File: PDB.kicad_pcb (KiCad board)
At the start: 2 copper layers, 50 x 80 mm, 98 parts, among them J1 Conn_01x02, J10 Conn_01x02_MountingPin, J11 USB_C_Receptacle_USB2.0, J2 Conn_01x02, J3 Conn_01x02, J4 Conn_01x02, J5 Conn_01x02, J6 Conn_01x02, J7 Conn_01x02, J8 Conn_01x02, J9 Conn_02x03_Odd_Even, SW1 SW_Push, U1 ATmega2560-16AU, U2 LMZM23600, U3 LTC2946, U4 FT230XQ, U5 LMZ13608, U6 LTC2946, Y1 16MHz

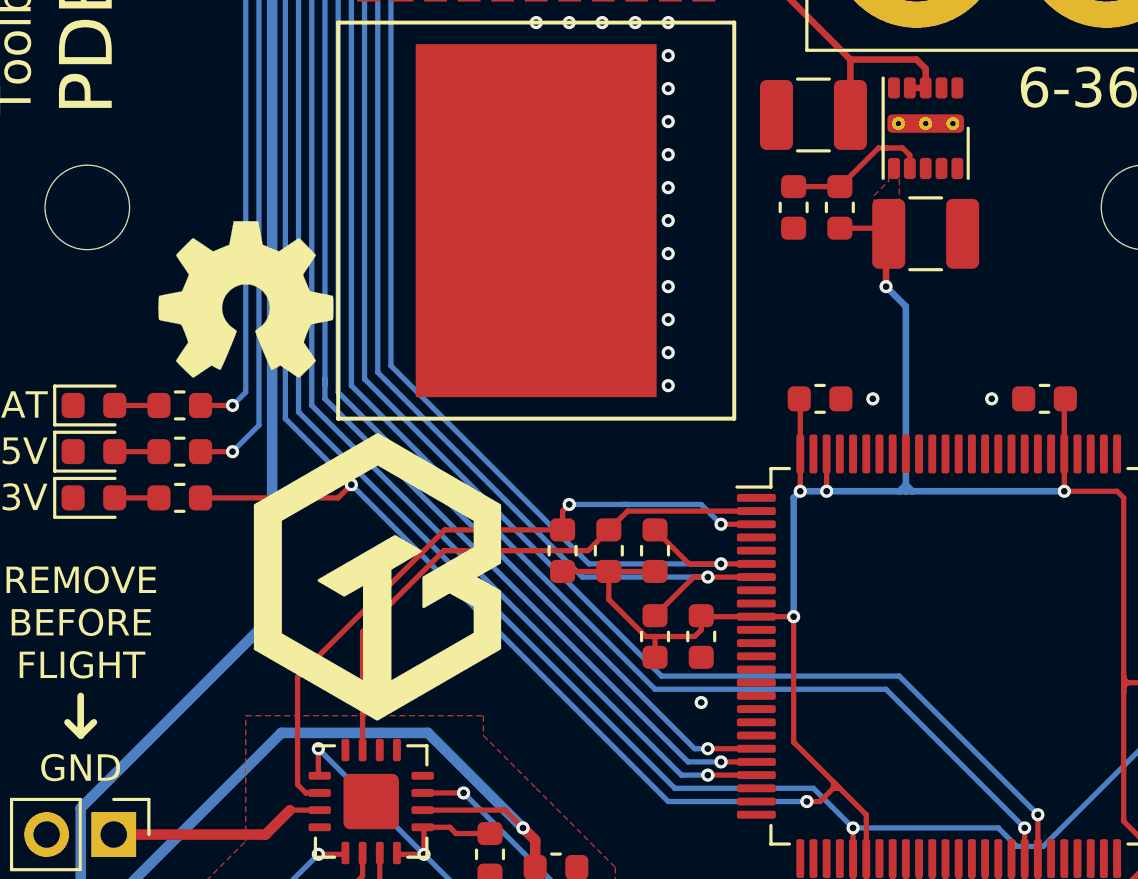
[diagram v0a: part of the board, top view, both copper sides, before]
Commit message: fix 3.3v regulator output cap
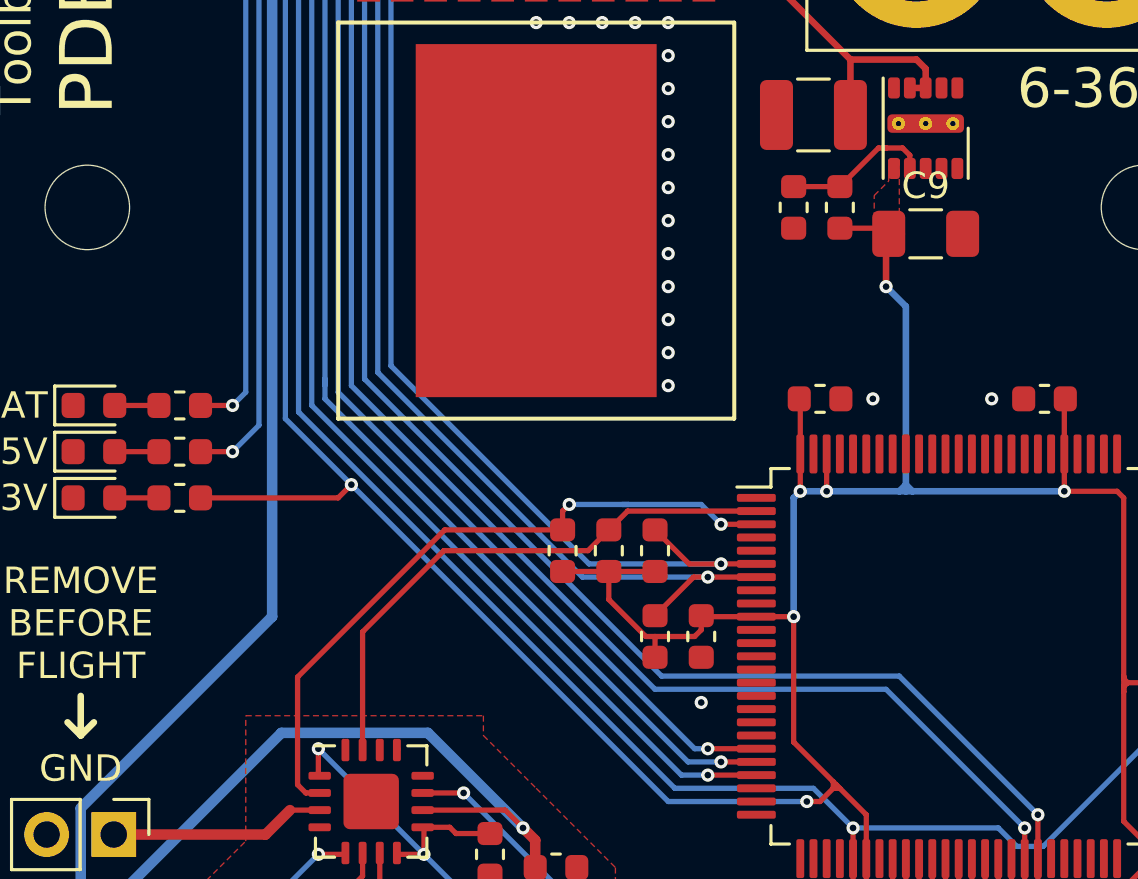
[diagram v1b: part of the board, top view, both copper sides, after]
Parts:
- removed REF**: OSHW-Symbol_6.7x6mm_SilkScreen, Symbol:OSHW-Symbol_6.7x6mm_SilkScreen
- removed REF**: ToolboxLogo_Large, Toolbox:ToolboxLogo_Large
- removed REF**: ToolboxLogo, Toolbox:ToolboxLogo
- C9: value 33µF -> 22µF; footprint Capacitor_SMD:C_1210_3225Metric -> Capacitor_SMD:C_1206_3216Metric

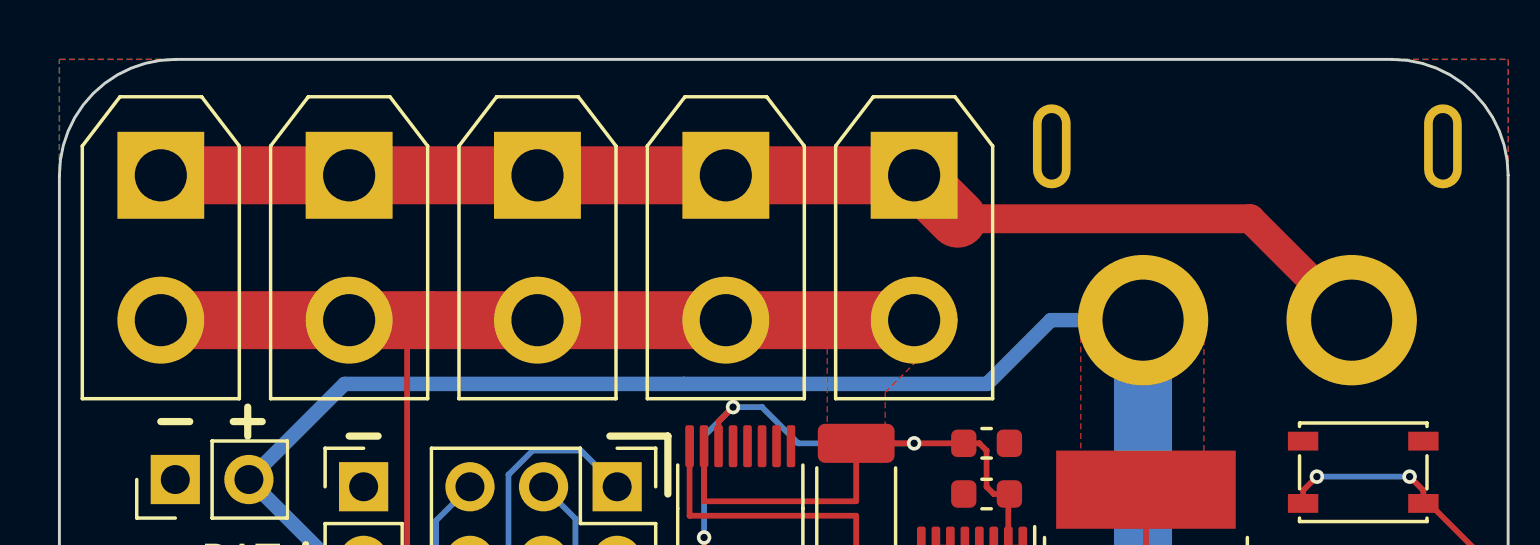
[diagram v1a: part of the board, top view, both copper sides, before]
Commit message: fix thermals for 5V out
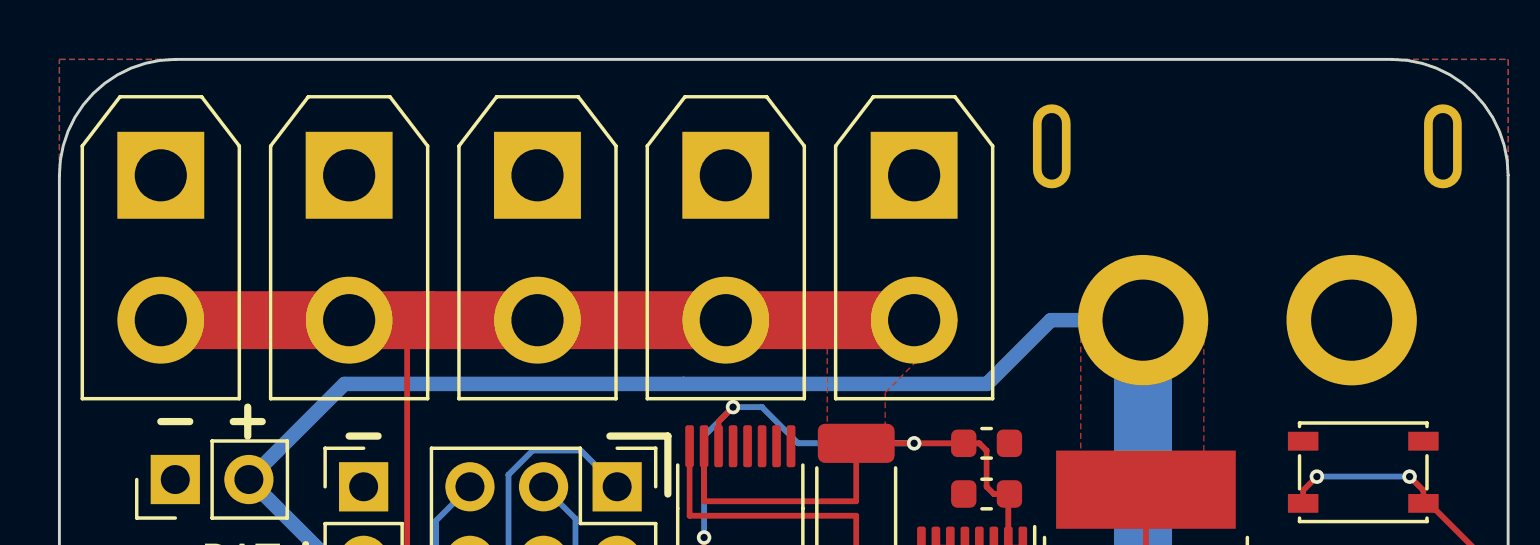
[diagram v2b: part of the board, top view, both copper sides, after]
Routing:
- net GND: track 43.2 -> 0.00 mm
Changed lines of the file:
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@@
     (thickness 1.6)
     (drawings 40)
-    (tracks 546)
+    (tracks 539)
     (zones 0)
     (modules 95)
@@
     (mod_text_size 1 1)
     (mod_text_width 0.25)
-    (pad_size 1.25 1.75)
-    (pad_drill 0)
+    (pad_size 3 3)
+    (pad_drill 1.8)
     (pad_to_mask_clearance 0)
     (solder_mask_min_width 0.25)
@@
       (net 21 +5V))
     (pad 1 thru_hole rect (at 0 0 270) (size 3 3) (drill 1.8) (layers *.Cu *.Mask)
-      (net 1 GND))
+      (net 1 GND) (thermal_width 1))
     (model ${KISYS3DMOD}/Connector_AMASS.3dshapes/AMASS_XT30UPB-F_1x02_P5.0mm_Vertical.wrl
       (at (xyz 0 0 0))
@@
       (net 21 +5V))
     (pad 1 thru_hole rect (at 0 0 270) (size 3 3) (drill 1.8) (layers *.Cu *.Mask)
-      (net 1 GND))
+      (net 1 GND) (thermal_width 1))
     (model ${KISYS3DMOD}/Connector_AMASS.3dshapes/AMASS_XT30UPB-F_1x02_P5.0mm_Vertical.wrl
       (at (xyz 0 0 0))
@@
       (net 21 +5V))
     (pad 1 thru_hole rect (at 0 0 270) (size 3 3) (drill 1.8) (layers *.Cu *.Mask)
-      (net 1 GND))
+      (net 1 GND) (thermal_width 1))
     (model ${KISYS3DMOD}/Connector_AMASS.3dshapes/AMASS_XT30UPB-F_1x02_P5.0mm_Vertical.wrl
       (at (xyz 0 0 0))
@@
       (net 21 +5V))
     (pad 1 thru_hole rect (at 0 0 270) (size 3 3) (drill 1.8) (layers *.Cu *.Mask)
-      (net 1 GND))
+      (net 1 GND) (thermal_width 1))
     (model ${KISYS3DMOD}/Connector_AMASS.3dshapes/AMASS_XT30UPB-F_1x02_P5.0mm_Vertical.wrl
       (at (xyz 0 0 0))
@@
       (net 21 +5V))
     (pad 1 thru_hole rect (at 0 0 270) (size 3 3) (drill 1.8) (layers *.Cu *.Mask)
-      (net 1 GND))
+      (net 1 GND) (thermal_width 1))
     (model ${KISYS3DMOD}/Connector_AMASS.3dshapes/AMASS_XT30UPB-F_1x02_P5.0mm_Vertical.wrl
       (at (xyz 0 0 0))
@@
   (via (at -39.5 19.75) (size 0.5) (drill 0.25) (layers F.Cu B.Cu) (net 1))
   (via (at -41.75 23) (size 0.5) (drill 0.25) (layers F.Cu B.Cu) (net 1))
-  (segment (start -46.5 4) (end -40 4) (width 2) (layer F.Cu) (net 1) (status 30))
-  (segment (start -40 4) (end -33.5 4) (width 2) (layer F.Cu) (net 1) (status 30))
-  (segment (start -33.5 4) (end -27 4) (width 2) (layer F.Cu) (net 1) (status 30))
-  (segment (start -5.4 9) (end -8.9 5.5) (width 1) (layer F.Cu) (net 1) (status 10))
-  (segment (start -8.9 5.5) (end -19.000001 5.499999) (width 1) (layer F.Cu) (net 1) (status 20))
-  (segment (start -27 4) (end -20.5 4) (width 2) (layer F.Cu) (net 1) (status 30))
-  (segment (start -20.5 4) (end -19.000001 5.499999) (width 2) (layer F.Cu) (net 1) (status 30))
   (via (at -23 33) (size 0.5) (drill 0.25) (layers F.Cu B.Cu) (net 1))
   (via (at -23 34.25) (size 0.5) (drill 0.25) (layers F.Cu B.Cu) (net 1))

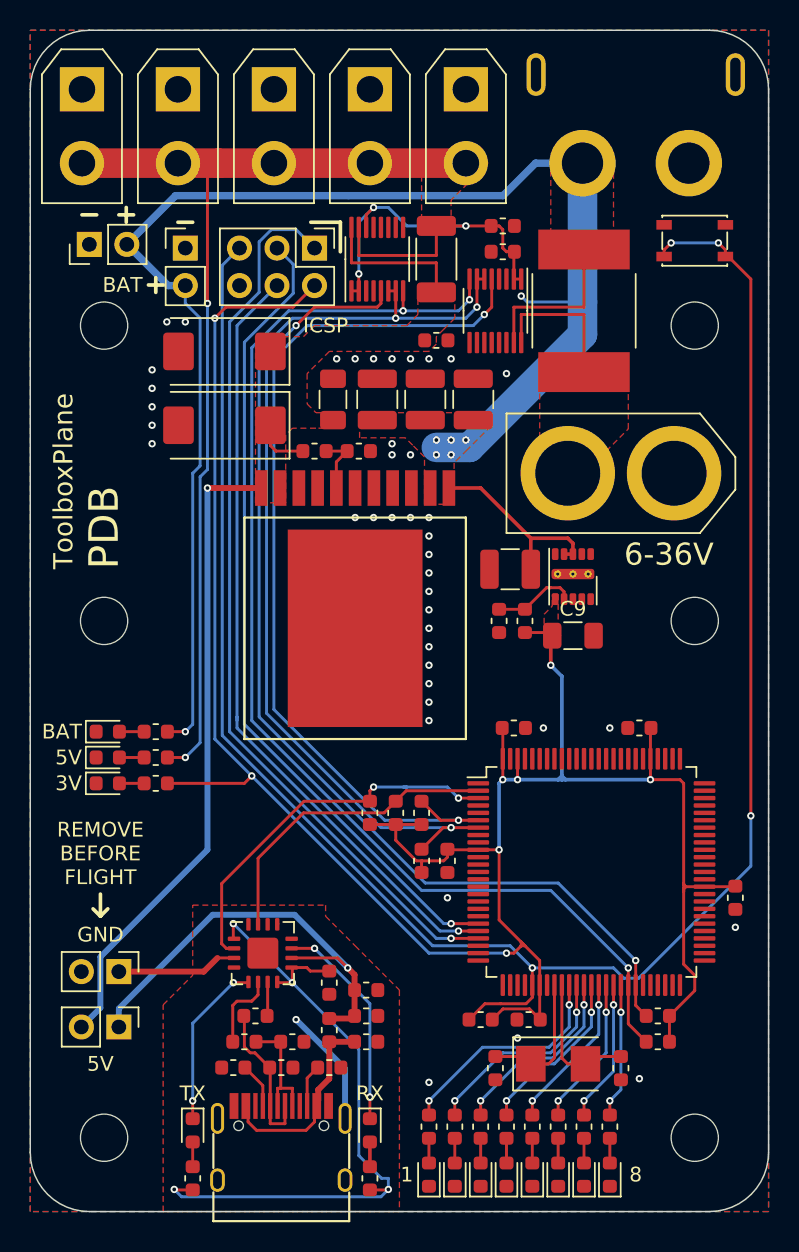
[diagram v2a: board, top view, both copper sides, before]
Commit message: layout fixes
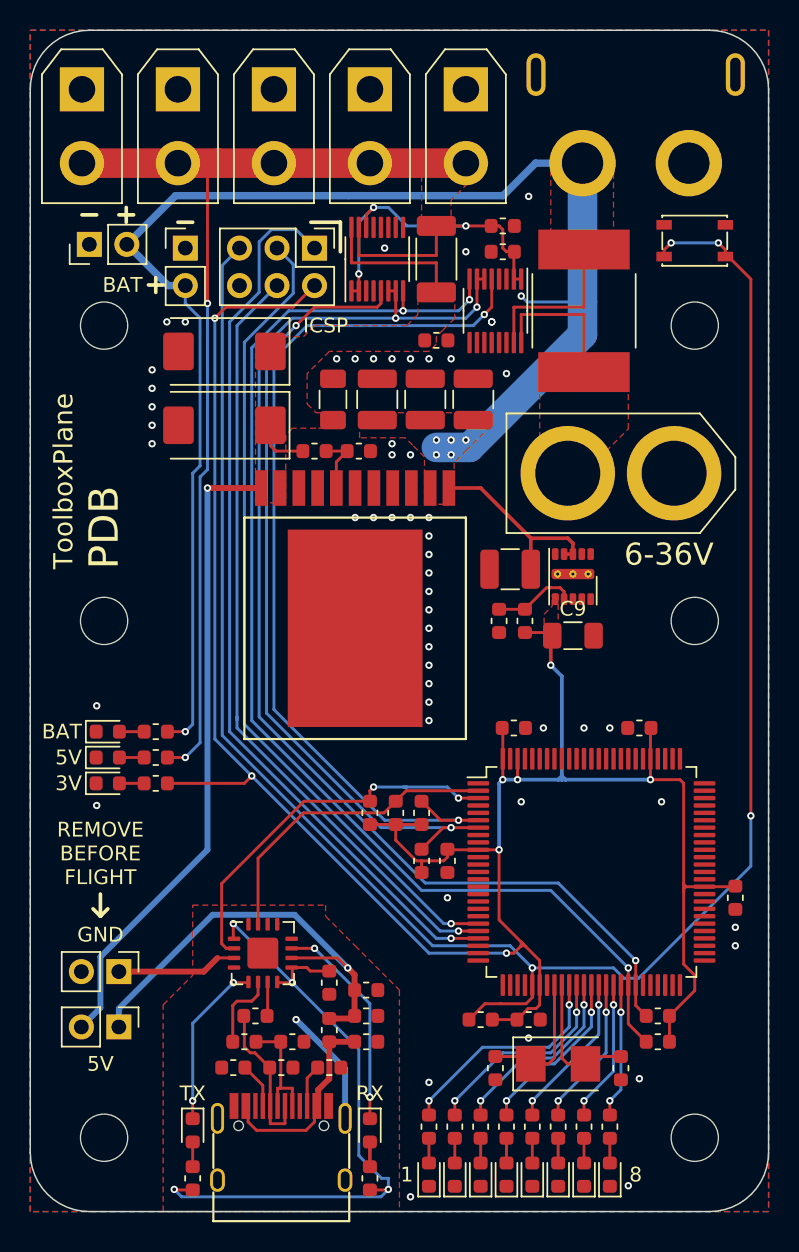
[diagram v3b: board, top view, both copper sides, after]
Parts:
- turned C7 to 180 degrees
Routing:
- net +3V3: track 161.5 -> 160.3 mm
- net GND: vias 41 -> 54
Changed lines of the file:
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@@
     (thickness 1.6)
     (drawings 40)
-    (tracks 539)
+    (tracks 552)
     (zones 0)
     (modules 95)
@@
     (mod_text_size 1 1)
     (mod_text_width 0.25)
-    (pad_size 3 3)
-    (pad_drill 1.8)
+    (pad_size 2.075 2.55)
+    (pad_drill 0)
     (pad_to_mask_clearance 0)
     (solder_mask_min_width 0.25)
@@
   )
   (module Capacitor_SMD:C_0603_1608Metric (layer F.Cu)
-    (at -16.25 67)
+    (at -16.25 67 180)
     (descr "Capacitor SMD 0603 (1608 Metric), square (rectangular) end terminal, IPC_7351 nominal, (Body size source: http://www.tortai-tech.com/upload/download/2011102023233369053.pdf), generated with kicad-footprint-generator")
     (tags capacitor)
     (attr smd)
-    (fp_text reference C7 (at 2.5 0) (layer F.SilkS) hide
+    (fp_text reference C7 (at 2.5 0 180) (layer F.SilkS) hide
       (effects (font (size 1 1) (thickness 0.15)))
     )
-    (fp_text value 100nF (at 0 1.43) (layer F.Fab)
+    (fp_text value 100nF (at 0 1.43 180) (layer F.Fab)
       (effects (font (size 1 1) (thickness 0.15)))
     )
-    (fp_text user %R (at 0 0) (layer F.Fab)
+    (fp_text user %R (at 0 0 180) (layer F.Fab)
       (effects (font (size 0.4 0.4) (thickness 0.06)))
     )
@@
     (fp_line (start -0.8 -0.4) (end 0.8 -0.4) (layer F.Fab) (width 0.1))
     (fp_line (start -0.8 0.4) (end -0.8 -0.4) (layer F.Fab) (width 0.1))
-    (pad 2 smd roundrect (at 0.7875 0) (size 0.875 0.95) (layers F.Cu F.Paste F.Mask) (roundrect_rratio 0.25)
+    (pad 2 smd roundrect (at 0.7875 0 180) (size 0.875 0.95) (layers F.Cu F.Paste F.Mask) (roundrect_rratio 0.25)
       (net 2 +3V3))
-    (pad 1 smd roundrect (at -0.7875 0) (size 0.875 0.95) (layers F.Cu F.Paste F.Mask) (roundrect_rratio 0.25)
+    (pad 1 smd roundrect (at -0.7875 0 180) (size 0.875 0.95) (layers F.Cu F.Paste F.Mask) (roundrect_rratio 0.25)
       (net 1 GND))
     (model ${KISYS3DMOD}/Capacitor_SMD.3dshapes/C_0603_1608Metric.wrl
@@
     (fp_line (start -1.6 1.25) (end -1.6 -1.25) (layer F.Fab) (width 0.1))
     (pad 2 smd roundrect (at 1.4 0 180) (size 1.25 2.65) (layers F.Cu F.Paste F.Mask) (roundrect_rratio 0.2)
-      (net 1 GND) (zone_connect 2))
+      (net 1 GND) (zone_connect 1) (thermal_width 1))
     (pad 1 smd roundrect (at -1.4 0 180) (size 1.25 2.65) (layers F.Cu F.Paste F.Mask) (roundrect_rratio 0.2)
       (net 37 +BATT) (zone_connect 2))
@@
     (fp_line (start -2.65 -2.15) (end -3.65 -1.15) (layer F.Fab) (width 0.1))
     (fp_line (start 3.65 -2.15) (end -2.65 -2.15) (layer F.Fab) (width 0.1))
-    (pad 2 smd roundrect (at 3.1125 0 180) (size 2.075 2.55) (layers F.Cu F.Paste F.Mask) (roundrect_rratio 0.120482)
-      (net 1 GND) (zone_connect 2))
+    (pad 2 smd roundrect (at 3.1125 0 180) (size 2.075 2.55) (layers F.Cu F.Paste F.Mask) (roundrect_rratio 0.12)
+      (net 1 GND) (zone_connect 1) (thermal_width 1))
     (pad 1 smd roundrect (at -3.1125 0 180) (size 2.075 2.55) (layers F.Cu F.Paste F.Mask) (roundrect_rratio 0.120482)
       (net 43 /5V/5VIN) (zone_connect 2))
@@
     (fp_line (start -2.65 -2.15) (end -3.65 -1.15) (layer F.Fab) (width 0.1))
     (fp_line (start 3.65 -2.15) (end -2.65 -2.15) (layer F.Fab) (width 0.1))
-    (pad 2 smd roundrect (at 3.1125 0 180) (size 2.075 2.55) (layers F.Cu F.Paste F.Mask) (roundrect_rratio 0.120482)
-      (net 1 GND) (zone_connect 2))
+    (pad 2 smd roundrect (at 3.1125 0 180) (size 2.075 2.55) (layers F.Cu F.Paste F.Mask) (roundrect_rratio 0.12)
+      (net 1 GND) (zone_connect 1) (thermal_width 1))
     (pad 1 smd roundrect (at -3.1125 0 180) (size 2.075 2.55) (layers F.Cu F.Paste F.Mask) (roundrect_rratio 0.120482)
       (net 43 /5V/5VIN) (zone_connect 2))
@@
   (via (at -10.75 47.25) (size 0.5) (drill 0.25) (layers F.Cu B.Cu) (net 1))
   (via (at -2.25 60.75) (size 0.5) (drill 0.25) (layers F.Cu B.Cu) (net 1))
-  (via (at -17 68.25) (size 0.5) (drill 0.25) (layers F.Cu B.Cu) (net 1))
+  (via (at -16.25 68.25) (size 0.5) (drill 0.25) (layers F.Cu B.Cu) (net 1))
   (via (at -8.75 71) (size 0.5) (drill 0.25) (layers F.Cu B.Cu) (net 1))
   (via (at -23 71.25) (size 0.5) (drill 0.25) (layers F.Cu B.Cu) (net 1))
   (via (at -21.75 58.75) (size 0.5) (drill 0.25) (layers F.Cu B.Cu) (net 1))
+  (via (at -12.5 47.25) (size 0.5) (drill 0.25) (layers F.Cu B.Cu) (net 1))
+  (via (at -2.25 62) (size 0.5) (drill 0.25) (layers F.Cu B.Cu) (net 1))
+  (via (at -24.25 79) (size 0.5) (drill 0.25) (layers F.Cu B.Cu) (net 1))
+  (via (at -9.5 78.25) (size 0.5) (drill 0.25) (layers F.Cu B.Cu) (net 1))
+  (via (at -45.5 45.75) (size 0.5) (drill 0.25) (layers F.Cu B.Cu) (net 1))
+  (via (at -45.5 52.5) (size 0.5) (drill 0.25) (layers F.Cu B.Cu) (net 1))
+  (via (at -26 14.75) (size 0.5) (drill 0.25) (layers F.Cu B.Cu) (net 1))
+  (via (at -18.75 19.75) (size 0.5) (drill 0.25) (layers F.Cu B.Cu) (net 1))
+  (via (at -18.75 19.75) (size 0.5) (drill 0.25) (layers F.Cu B.Cu) (net 1))
+  (via (at -16.25 11.25) (size 0.5) (drill 0.25) (layers F.Cu B.Cu) (net 1))
+  (via (at -20.5 15) (size 0.5) (drill 0.25) (layers F.Cu B.Cu) (net 1))
+  (via (at -7.25 52.25) (size 0.5) (drill 0.25) (layers F.Cu B.Cu) (net 1))
+  (via (at -16.75 52.25) (size 0.5) (drill 0.25) (layers F.Cu B.Cu) (net 1))
   (segment (start -2.2875 58) (end -2.25 57.9625) (width 0.2) (layer F.Cu) (net 2) (status 30))
   (segment (start -4.3375 58) (end -2.2875 58) (width 0.2) (layer F.Cu) (net 2) (status 30))
@@
   (segment (start -17 50.75) (end -14.25 50.75) (width 0.25) (layer B.Cu) (net 2))
   (segment (start -14.25 50.75) (end -14 50.75) (width 0.25) (layer B.Cu) (net 2))
-  (segment (start -17.98749 66.27499) (end -16.18751 66.27499) (width 0.2) (layer F.Cu) (net 2))
-  (segment (start -16.18751 66.27499) (end -15.4625 67) (width 0.2) (layer F.Cu) (net 2) (status 20))
-  (segment (start -18.7125 67) (end -17.98749 66.27499) (width 0.2) (layer F.Cu) (net 2) (status 10))
-  (segment (start -15.5 66.9625) (end -15.4625 67) (width 0.2) (layer F.Cu) (net 2) (status 30))
-  (segment (start -15.5 64.6625) (end -15.5 66.9625) (width 0.2) (layer F.Cu) (net 2) (status 30))
   (segment (start -6.7125 68.5) (end -6.7125 66.75) (width 0.2) (layer F.Cu) (net 2) (status 30))
   (segment (start -5.75 63.25) (end -5 64) (width 0.2) (layer F.Cu) (net 2))
@@
   (segment (start -37.5 48) (end -35 50.5) (width 0.2) (layer B.Cu) (net 2))
   (segment (start -40.7125 51) (end -35.5 51) (width 0.2) (layer F.Cu) (net 2) (status 10))
+  (segment (start -17.0375 67) (end -18.7125 67) (width 0.2) (layer F.Cu) (net 2))
+  (segment (start -17.0375 67) (end -16.2875 66.25) (width 0.2) (layer F.Cu) (net 2))
+  (segment (start -16.2875 66.25) (end -15.75 66.25) (width 0.2) (layer F.Cu) (net 2))
+  (segment (start -15.5 66) (end -15.5 64.6625) (width 0.2) (layer F.Cu) (net 2))
+  (segment (start -15.75 66.25) (end -15.5 66) (width 0.2) (layer F.Cu) (net 2))
   (segment (start -16.75 21.15) (end -16.75 19.25) (width 0.2) (layer F.Cu) (net 3) (status 10))
   (segment (start -12.5 19.25) (end -12.5 23.15) (width 0.2) (layer F.Cu) (net 3) (status 20))
